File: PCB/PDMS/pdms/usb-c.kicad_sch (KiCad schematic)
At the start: 10 parts, among them J6 2305018-2, U12 USBLC6-2SC6

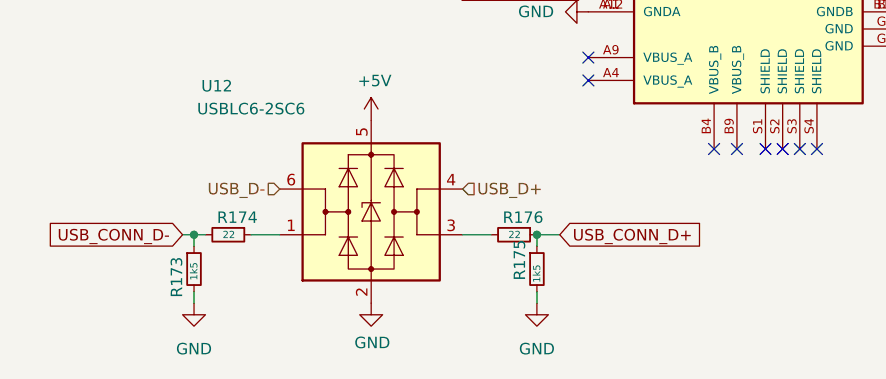
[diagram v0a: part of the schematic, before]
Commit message: USB-C symbol changed
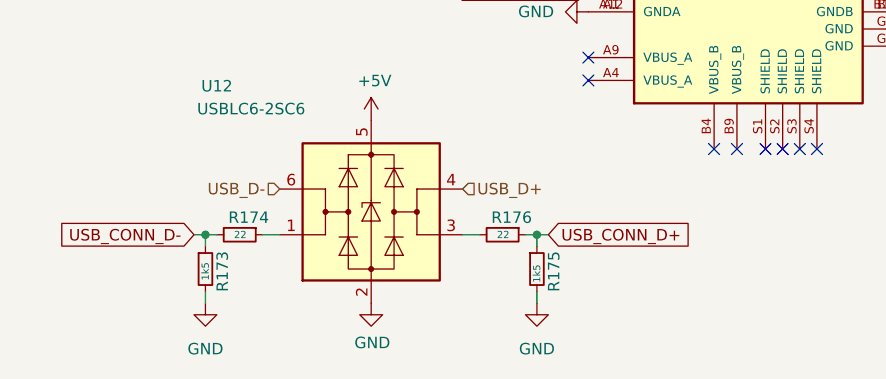
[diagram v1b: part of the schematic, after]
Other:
- moved on the sheet: R173, R174, R176
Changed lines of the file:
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@@
 (kicad_sch (version 20211123) (generator eeschema)
   (paper "A5")
-  (junction (at 41.275 91.44) (diameter 0) (color 0 0 0 0)
+  (junction (at 42.545 91.44) (diameter 0) (color 0 0 0 0)
   )
   (junction (at 79.375 91.44) (diameter 0) (color 0 0 0 0)
@@
   (no_connect (at 85.09 71.755))
   (no_connect (at 85.09 74.295))
+  (wire (pts (xy 78.105 91.44) (xy 79.375 91.44))
+    (stroke (width 0) (type default) (color 0 0 0 0))
+  )
+  (wire (pts (xy 42.545 91.44) (xy 42.545 92.71))
+    (stroke (width 0) (type default) (color 0 0 0 0))
+  )
   (wire (pts (xy 83.185 51.435) (xy 85.09 51.435))
     (stroke (width 0) (type default) (color 0 0 0 0))
   )
-  (wire (pts (xy 50.8 91.44) (xy 47.625 91.44))
+  (wire (pts (xy 50.8 91.44) (xy 48.895 91.44))
     (stroke (width 0) (type default) (color 0 0 0 0))
   )
@@
     (stroke (width 0) (type default) (color 0 0 0 0))
   )
-  (wire (pts (xy 71.12 91.44) (xy 74.295 91.44))
-    (stroke (width 0) (type default) (color 0 0 0 0))
-  )
-  (wire (pts (xy 41.275 97.79) (xy 41.275 99.06))
+  (wire (pts (xy 71.12 91.44) (xy 73.025 91.44))
+    (stroke (width 0) (type default) (color 0 0 0 0))
+  )
+  (wire (pts (xy 42.545 97.79) (xy 42.545 99.06))
     (stroke (width 0) (type default) (color 0 0 0 0))
   )
@@
     (stroke (width 0) (type default) (color 0 0 0 0))
   )
-  (wire (pts (xy 41.275 91.44) (xy 40.005 91.44))
-    (stroke (width 0) (type default) (color 0 0 0 0))
-  )
   (wire (pts (xy 41.91 55.88) (xy 43.815 55.88))
     (stroke (width 0) (type default) (color 0 0 0 0))
   )
-  (wire (pts (xy 41.275 91.44) (xy 41.275 92.71))
-    (stroke (width 0) (type default) (color 0 0 0 0))
-  )
-  (wire (pts (xy 81.915 91.44) (xy 79.375 91.44))
+  (wire (pts (xy 80.645 91.44) (xy 79.375 91.44))
     (stroke (width 0) (type default) (color 0 0 0 0))
   )
@@
     (stroke (width 0) (type default) (color 0 0 0 0))
   )
-  (wire (pts (xy 42.545 91.44) (xy 41.275 91.44))
+  (wire (pts (xy 41.275 91.44) (xy 42.545 91.44))
     (stroke (width 0) (type default) (color 0 0 0 0))
   )
   (wire (pts (xy 122.555 51.435) (xy 120.65 51.435))
+    (stroke (width 0) (type default) (color 0 0 0 0))
+  )
+  (wire (pts (xy 42.545 91.44) (xy 43.815 91.44))
     (stroke (width 0) (type default) (color 0 0 0 0))
   )
@@
     )
   )
-  (global_label "USB_CONN_D+" (shape input) (at 81.915 91.44 0) (fields_autoplaced)
-    (effects (font (size 1.27 1.27)) (justify left))
-    (property "Intersheet References" "${INTERSHEET_REFS}" (id 0) (at -57.785 -77.47 0)
+  (global_label "USB_CONN_D+" (shape input) (at 80.645 91.44 0) (fields_autoplaced)
+    (effects (font (size 1.27 1.27)) (justify left))
+    (property "Intersheet References" "${INTERSHEET_REFS}" (id 0) (at -59.055 -77.47 0)
       (effects (font (size 1.27 1.27)) (justify right) hide)
     )
@@
     )
   )
-  (global_label "USB_CONN_D-" (shape input) (at 40.005 91.44 180) (fields_autoplaced)
-    (effects (font (size 1.27 1.27)) (justify right))
-    (property "Intersheet References" "${INTERSHEET_REFS}" (id 0) (at -79.375 -77.47 0)
+  (global_label "USB_CONN_D-" (shape input) (at 41.275 91.44 180) (fields_autoplaced)
+    (effects (font (size 1.27 1.27)) (justify right))
+    (property "Intersheet References" "${INTERSHEET_REFS}" (id 0) (at -78.105 -77.47 0)
       (effects (font (size 1.27 1.27)) (justify right) hide)
     )
@@
     (pin "2")
   )
-  (symbol (lib_id "Device:R_Small") (at 41.275 95.25 0) (unit 1)
-    (in_bom yes) (on_board yes)
-    (property "Reference" "R173" (id 0) (at 39.37 98.425 90)
-      (effects (font (size 1.27 1.27)) (justify left))
-    )
-    (property "Value" "1k5" (id 1) (at 41.275 96.52 90)
-      (effects (font (size 0.8 0.8)) (justify left))
-    )
-    (property "Footprint" "Resistor_SMD:R_0402_1005Metric" (id 2) (at 41.275 95.25 0)
-      (effects (font (size 1.27 1.27)) hide)
-    )
-    (property "Datasheet" "~" (id 3) (at 41.275 95.25 0)
+  (symbol (lib_id "Device:R_Small") (at 42.545 95.25 0) (unit 1)
+    (in_bom yes) (on_board yes)
+    (property "Reference" "R173" (id 0) (at 44.45 97.79 90)
+      (effects (font (size 1.27 1.27)) (justify left))
+    )
+    (property "Value" "1k5" (id 1) (at 42.545 96.52 90)
+      (effects (font (size 0.8 0.8)) (justify left))
+    )
+    (property "Footprint" "Resistor_SMD:R_0402_1005Metric" (id 2) (at 42.545 95.25 0)
+      (effects (font (size 1.27 1.27)) hide)
+    )
+    (property "Datasheet" "~" (id 3) (at 42.545 95.25 0)
       (effects (font (size 1.27 1.27)) hide)
     )
@@
     (pin "1")
   )
-  (symbol (lib_id "power:GND") (at 41.275 99.06 0) (unit 1)
-    (in_bom yes) (on_board yes) (fields_autoplaced)
-    (property "Reference" "#PWR0398" (id 0) (at 41.275 105.41 0)
-      (effects (font (size 1.27 1.27)) hide)
-    )
-    (property "Value" "GND" (id 1) (at 41.275 104.14 0))
-    (property "Footprint" "" (id 2) (at 41.275 99.06 0)
-      (effects (font (size 1.27 1.27)) hide)
-    )
-    (property "Datasheet" "" (id 3) (at 41.275 99.06 0)
+  (symbol (lib_id "power:GND") (at 42.545 99.06 0) (unit 1)
+    (in_bom yes) (on_board yes) (fields_autoplaced)
+    (property "Reference" "#PWR0398" (id 0) (at 42.545 105.41 0)
+      (effects (font (size 1.27 1.27)) hide)
+    )
+    (property "Value" "GND" (id 1) (at 42.545 104.14 0))
+    (property "Footprint" "" (id 2) (at 42.545 99.06 0)
+      (effects (font (size 1.27 1.27)) hide)
+    )
+    (property "Datasheet" "" (id 3) (at 42.545 99.06 0)
       (effects (font (size 1.27 1.27)) hide)
     )
@@
     (pin "2")
   )
-  (symbol (lib_id "Device:R_Small") (at 76.835 91.44 270) (unit 1)
-    (in_bom yes) (on_board yes)
-    (property "Reference" "R176" (id 0) (at 75.565 89.535 90)
-      (effects (font (size 1.27 1.27)) (justify left))
-    )
-    (property "Value" "22" (id 1) (at 76.2 91.44 90)
-      (effects (font (size 0.8 0.8)) (justify left))
-    )
-    (property "Footprint" "Resistor_SMD:R_0402_1005Metric" (id 2) (at 76.835 91.44 0)
-      (effects (font (size 1.27 1.27)) hide)
-    )
-    (property "Datasheet" "~" (id 3) (at 76.835 91.44 0)
+  (symbol (lib_id "Device:R_Small") (at 75.565 91.44 270) (unit 1)
+    (in_bom yes) (on_board yes)
+    (property "Reference" "R176" (id 0) (at 74.295 89.535 90)
+      (effects (font (size 1.27 1.27)) (justify left))
+    )
+    (property "Value" "22" (id 1) (at 74.93 91.44 90)
+      (effects (font (size 0.8 0.8)) (justify left))
+    )
+    (property "Footprint" "Resistor_SMD:R_0402_1005Metric" (id 2) (at 75.565 91.44 0)
+      (effects (font (size 1.27 1.27)) hide)
+    )
+    (property "Datasheet" "~" (id 3) (at 75.565 91.44 0)
       (effects (font (size 1.27 1.27)) hide)
     )
@@
     (pin "2")
   )
-  (symbol (lib_id "Device:R_Small") (at 45.085 91.44 270) (unit 1)
-    (in_bom yes) (on_board yes)
-    (property "Reference" "R174" (id 0) (at 43.815 89.535 90)
-      (effects (font (size 1.27 1.27)) (justify left))
-    )
-    (property "Value" "22" (id 1) (at 44.45 91.44 90)
-      (effects (font (size 0.8 0.8)) (justify left))
-    )
-    (property "Footprint" "Resistor_SMD:R_0402_1005Metric" (id 2) (at 45.085 91.44 0)
-      (effects (font (size 1.27 1.27)) hide)
-    )
-    (property "Datasheet" "~" (id 3) (at 45.085 91.44 0)
+  (symbol (lib_id "Device:R_Small") (at 46.355 91.44 270) (unit 1)
+    (in_bom yes) (on_board yes)
+    (property "Reference" "R174" (id 0) (at 45.085 89.535 90)
+      (effects (font (size 1.27 1.27)) (justify left))
+    )
+    (property "Value" "22" (id 1) (at 45.72 91.44 90)
+      (effects (font (size 0.8 0.8)) (justify left))
+    )
+    (property "Footprint" "Resistor_SMD:R_0402_1005Metric" (id 2) (at 46.355 91.44 0)
+      (effects (font (size 1.27 1.27)) hide)
+    )
+    (property "Datasheet" "~" (id 3) (at 46.355 91.44 0)
       (effects (font (size 1.27 1.27)) hide)
     )
@@
   (symbol (lib_id "Device:R_Small") (at 79.375 95.25 0) (unit 1)
     (in_bom yes) (on_board yes)
-    (property "Reference" "R175" (id 0) (at 77.47 96.52 90)
-      (effects (font (size 1.27 1.27)) (justify left))
-    )
+    (property "Reference" "R175" (id 0) (at 81.28 97.79 90)
+      (effects (font (size 1.27 1.27)) (justify left))
+    )
